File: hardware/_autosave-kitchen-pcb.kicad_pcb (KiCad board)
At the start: 4 copper layers, 82.6 x 82.5 mm, 84 parts, among them J1 MEM2075-00-140-01-A, J2 Conn_02x02_Odd_Even, J3 Conn_01x06, J4 S3B-XH-SM4-TB_LF__SN_, J5 DCJ200-10-A-K1-K, J6 USB4105-GF-A, Q1 TEMT6000X01, SW1 RA1113112R, SW2 SW_Push, SW3 SW_Push, U1 SHT30-DIS-B, U2 MX25L3233FM2I-08G, U3 NCP1117ST33T3G, U4 ESP32-S3-WROOM-1-N8R8, U5 USBLC6-2SC6

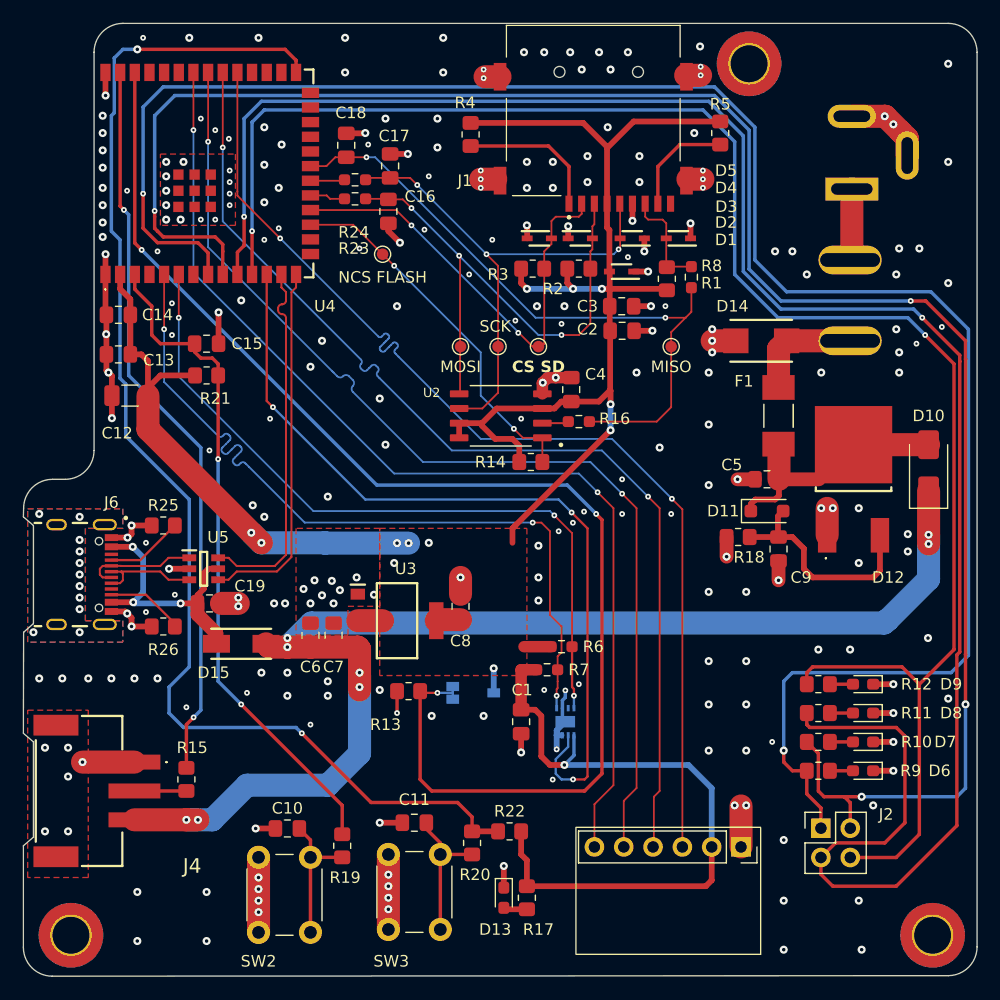
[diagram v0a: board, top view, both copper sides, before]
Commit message: DFM ready PCB no silkscreen
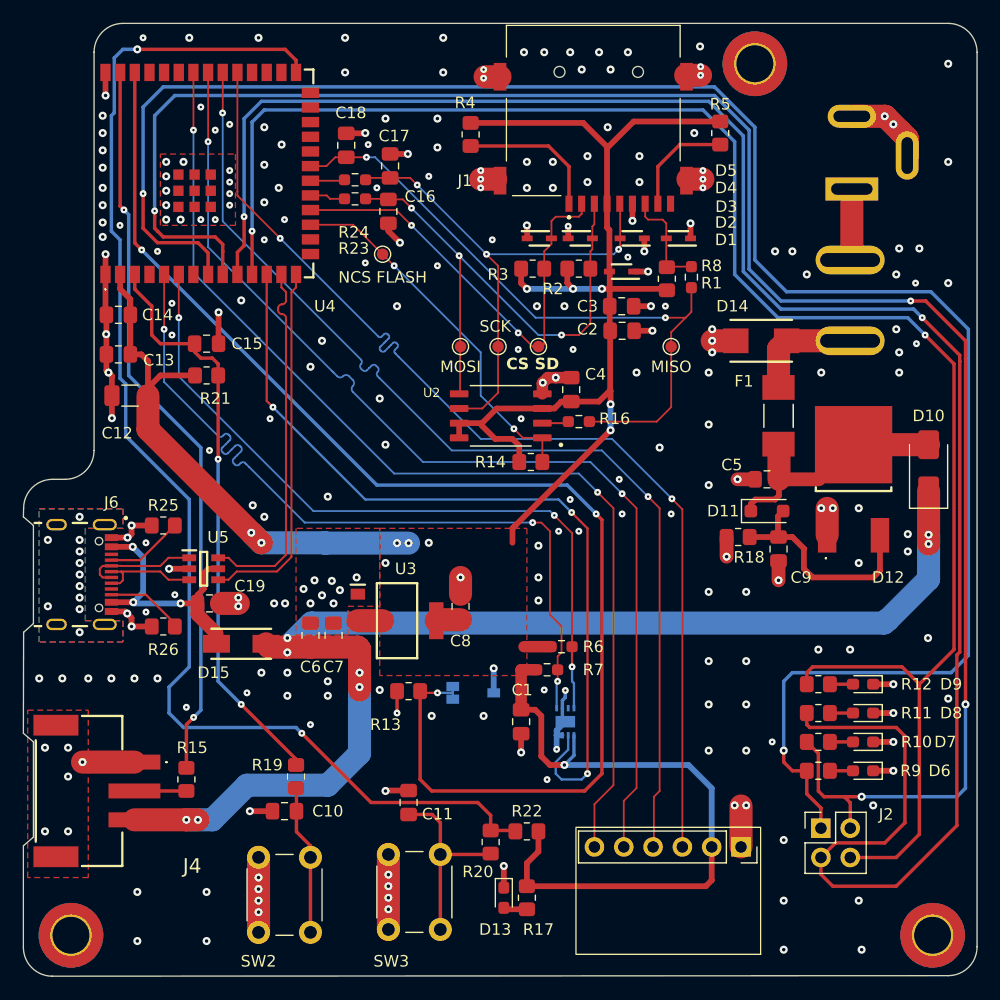
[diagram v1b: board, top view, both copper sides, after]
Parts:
- moved R19 7.21 mm to (121.0, 123.8)
- moved C11 1.82 mm to (130.8, 126.0), turned to -90 degrees
- moved R20 1.61 mm to (137.9, 129.4)
- moved C10 1.52 mm to (120.0, 126.8)
- moved R22 1.50 mm to (141.0, 128.5)
- moved H3 0.50 mm to (160.8, 62.0)
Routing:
- net /ESP32/EN: track 58.3 -> 50.6 mm
- net Net-(C11-Pad2): track 12.5 -> 16.7 mm
- net /ESP32/BOOT: track 111.4 -> 112.9 mm
- net Net-(C10-Pad2): track 12.2 -> 13.1 mm
- net GND: track 116.8 -> 117.1 mm, vias 264 -> 262
